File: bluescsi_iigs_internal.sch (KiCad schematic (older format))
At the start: 21 parts, among them J1 Conn_02x13_Odd_Even, J2 Conn_02x13_Odd_Even, J3 105162-0001, J4 Conn_01x02_Male, SW1 SW_SPDT, U1 YAAJ_BluePill, U2 UCC5606, U3 UCC5606, U4 AMS1117-5.0

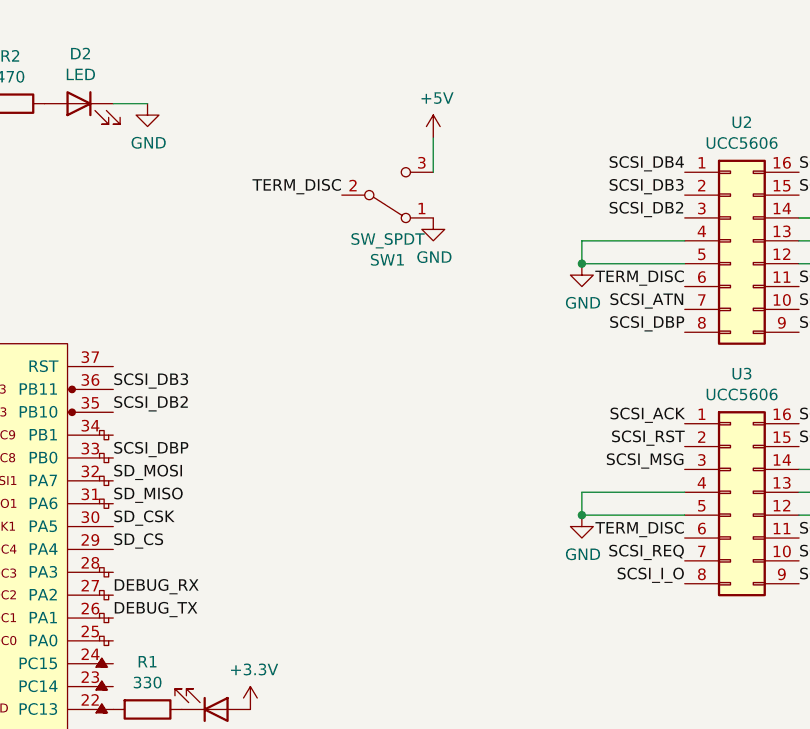
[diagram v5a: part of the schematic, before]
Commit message: Add JPs to set the DISCNT signal level for compatibility with UC560x, UCC560x and UCC5612 terminator ICs
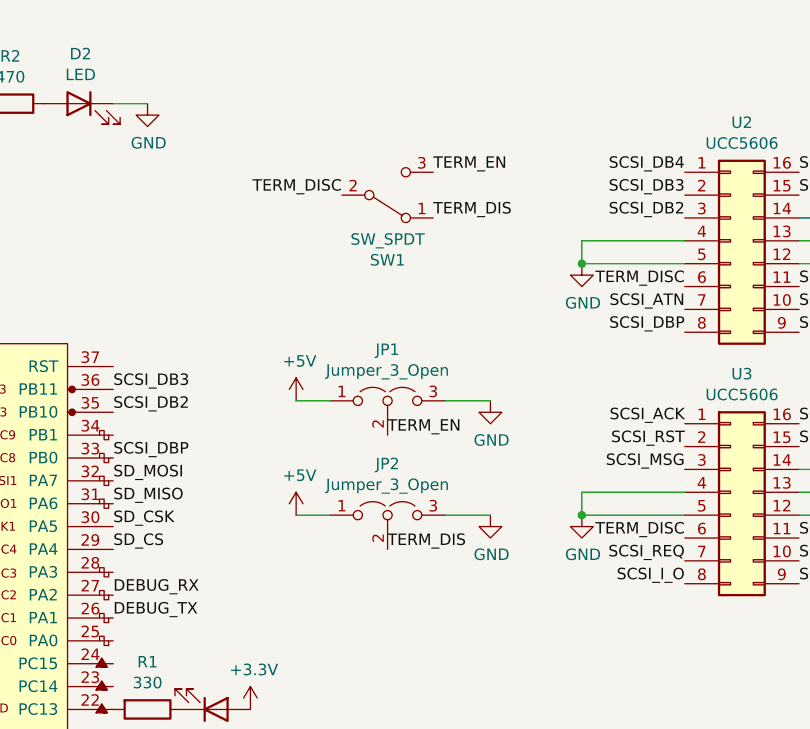
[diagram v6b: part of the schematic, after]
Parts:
- added JP1, JP2: Jumper_3_Open, Jumper:SolderJumper-3_P1.3mm_Open_Pad1.0x1.5mm_NumberLabels, symbol Jumper:Jumper_3_Open
- J3: footprint 105162-0001 -> Molex 105162-0001:105162-0001
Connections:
- net +5V: now also JP1.1 (A), JP2.1 (A); no longer SW1.3 (C)
- net GND: now also JP1.3 (B), JP2.3 (B); no longer SW1.1 (A)
- new net TERM_DIS: JP2.2 (C), SW1.1 (A)
- new net TERM_EN: JP1.2 (C), SW1.3 (C)
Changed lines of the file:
@@
 Text Label 7100 1300 2    50   ~ 0
 TERM_DISC
-$Comp
-L power:GND #PWR0118
-U 1 1 606D8850
-P 7500 1400
-F 0 "#PWR0118" H 7500 1150 50  0001 C CNN
-F 1 "GND" H 7505 1227 50  0000 C CNN
-F 2 "" H 7500 1400 50  0001 C CNN
-F 3 "" H 7500 1400 50  0001 C CNN
-	1    7500 1400
-	1    0    0    -1
-$EndComp
-$Comp
-L power:+5V #PWR0112
-U 1 1 60708B21
-P 7500 1050
-F 0 "#PWR0112" H 7500 900 50  0001 C CNN
-F 1 "+5V" H 7515 1223 50  0000 C CNN
-F 2 "" H 7500 1050 50  0001 C CNN
-F 3 "" H 7500 1050 50  0001 C CNN
-	1    7500 1050
-	1    0    0    -1
-$EndComp
 Text Label 1100 2800 2    50   ~ 0
 SCSI_REQ
@@
 	3300 1300 3300 1050
 Connection ~ 3300 1300
-Wire Wire Line
-	7500 1200 7500 1050
 Text Label 6100 3150 0    50   ~ 0
 DEBUG_TX
@@
 F 0 "J3" H 4650 5267 50  0000 C CNN
 F 1 "105162-0001" H 4650 5176 50  0000 C CNN
-F 2 "105162-0001" H 4000 5000 50  0001 L BNN
+F 2 "Molex 105162-0001:105162-0001" H 4000 5000 50  0001 L BNN
 F 3 "" H 4000 5000 50  0001 L BNN
 F 4 "Memory Card Connectors 1.45H MICRO SD HEADER WITH D/C PIN" H 4000 5000 50  0001 L BNN "DESCRIPTION"
@@
 Wire Wire Line
 	4000 5500 3600 5500
+$Comp
+L Jumper:Jumper_3_Open JP1
+U 1 1 608B8175
+P 7300 2200
+F 0 "JP1" H 7300 2424 50  0000 C CNN
+F 1 "Jumper_3_Open" H 7300 2333 50  0000 C CNN
+F 2 "Jumper:SolderJumper-3_P1.3mm_Open_Pad1.0x1.5mm_NumberLabels" H 7300 2200 50  0001 C CNN
+F 3 "~" H 7300 2200 50  0001 C CNN
+	1    7300 2200
+	1    0    0    -1
+$EndComp
+$Comp
+L Jumper:Jumper_3_Open JP2
+U 1 1 608B8DEE
+P 7300 2700
+F 0 "JP2" H 7300 2924 50  0000 C CNN
+F 1 "Jumper_3_Open" H 7300 2833 50  0000 C CNN
+F 2 "Jumper:SolderJumper-3_P1.3mm_Open_Pad1.0x1.5mm_NumberLabels" H 7300 2700 50  0001 C CNN
+F 3 "~" H 7300 2700 50  0001 C CNN
+	1    7300 2700
+	1    0    0    -1
+$EndComp
+Text Label 7300 2350 0    50   ~ 0
+TERM_EN
+Text Label 7300 2850 0    50   ~ 0
+TERM_DIS
+$Comp
+L power:+5V #PWR0112
+U 1 1 608BB349
+P 6900 2200
+F 0 "#PWR0112" H 6900 2050 50  0001 C CNN
+F 1 "+5V" H 6915 2373 50  0000 C CNN
+F 2 "" H 6900 2200 50  0001 C CNN
+F 3 "" H 6900 2200 50  0001 C CNN
+	1    6900 2200
+	1    0    0    -1
+$EndComp
+$Comp
+L power:+5V #PWR0118
+U 1 1 608BC12D
+P 6900 2700
+F 0 "#PWR0118" H 6900 2550 50  0001 C CNN
+F 1 "+5V" H 6915 2873 50  0000 C CNN
+F 2 "" H 6900 2700 50  0001 C CNN
+F 3 "" H 6900 2700 50  0001 C CNN
+	1    6900 2700
+	1    0    0    -1
+$EndComp
+$Comp
+L power:GND #PWR0122
+U 1 1 608BCCDB
+P 7750 2200
+F 0 "#PWR0122" H 7750 1950 50  0001 C CNN
+F 1 "GND" H 7755 2027 50  0000 C CNN
+F 2 "" H 7750 2200 50  0001 C CNN
+F 3 "" H 7750 2200 50  0001 C CNN
+	1    7750 2200
+	1    0    0    -1
+$EndComp
+$Comp
+L power:GND #PWR0124
+U 1 1 608BD849
+P 7750 2700
+F 0 "#PWR0124" H 7750 2450 50  0001 C CNN
+F 1 "GND" H 7755 2527 50  0000 C CNN
+F 2 "" H 7750 2700 50  0001 C CNN
+F 3 "" H 7750 2700 50  0001 C CNN
+	1    7750 2700
+	1    0    0    -1
+$EndComp
+Wire Wire Line
+	6900 2200 7050 2200
+Wire Wire Line
+	6900 2700 7050 2700
+Wire Wire Line
+	7550 2700 7750 2700
+Wire Wire Line
+	7550 2200 7750 2200
+Text Label 7500 1200 0    50   ~ 0
+TERM_EN
+Text Label 7500 1400 0    50   ~ 0
+TERM_DIS
 $EndSCHEMATC
